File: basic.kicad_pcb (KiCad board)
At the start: 4 copper layers, 60 x 80 mm, 96 parts, among them CON1 MSATA-PCIE_MINI-CARD-MM60-52B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, J2 simcard, J3 Conn_01x02_Male, J4 Conn_01x02_Male, J5 Conn_02x02_Top_Bottom, Q1 DMP3099L-7, Q3 MBT3904DW1, SW1 SW_Push, U1 ESP32-WROOM-32U, U2 MCP2515-QFN, U3 TPS565201DDC, U4 TCAN332, U5 MCP73223-C2S, U6 MIC94085, U7 MMA8452Q, U8 TPS22810DRV, U9 TC2030_SWD, X1 dummy, X2 dummy, Y2 M8AIG-16-12-2T3

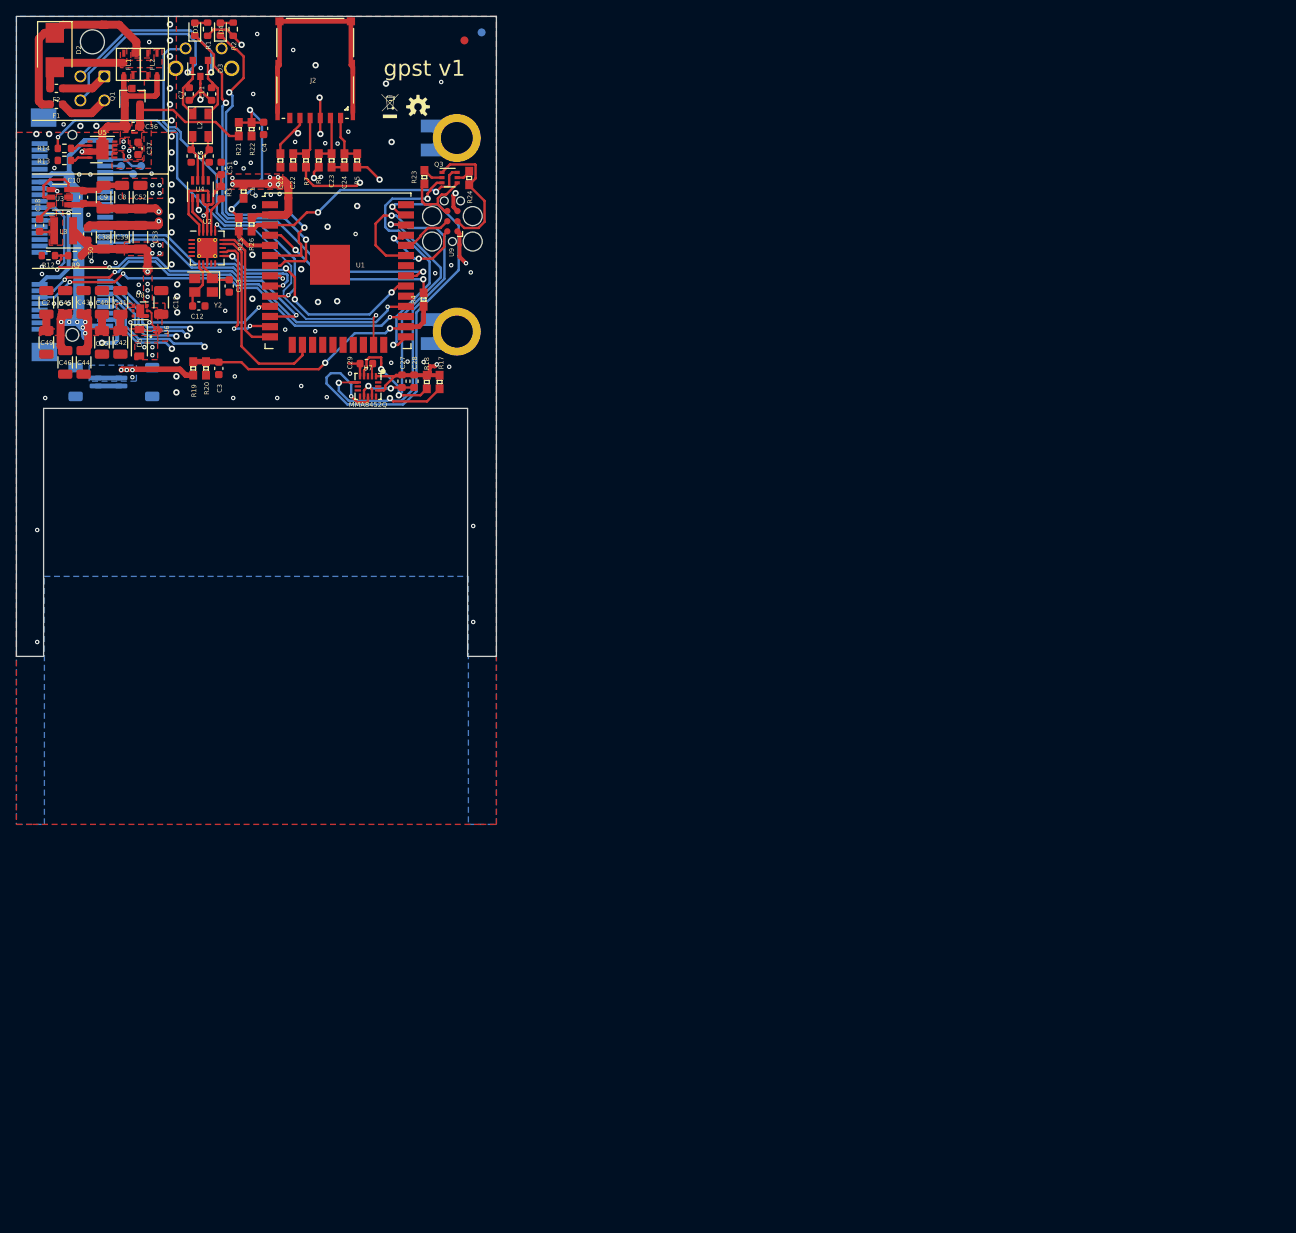
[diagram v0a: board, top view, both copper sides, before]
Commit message: Power section placement completed.
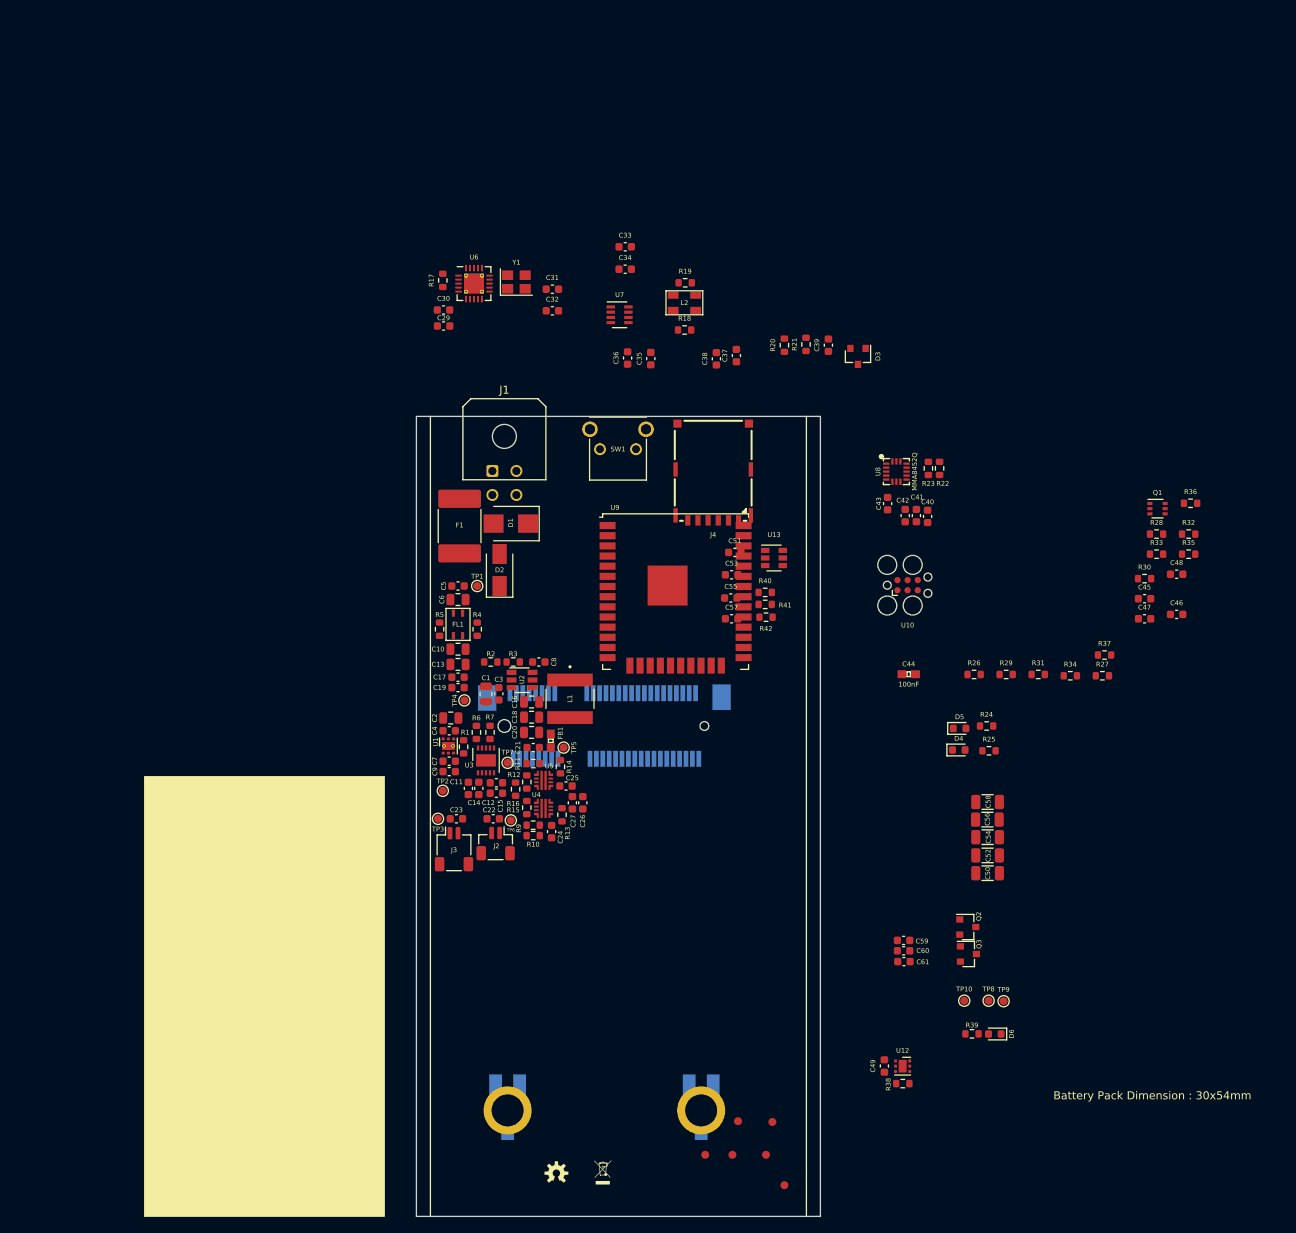
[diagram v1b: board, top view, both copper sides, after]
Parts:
- removed C28: 0.1uF, Capacitor_SMD:C_0603_1608Metric
- removed F2: C2Q 4, Fuse:Fuse_0603_1608Metric
- removed FL2: BACKUP ACP3225-501-2P-T000, aep:ACP3225
- removed J5: Conn_02x02_Top_Bottom, Connector_Molex:Molex_Micro-Fit_3.0_43045-0400_2x02_P3.00mm_Horizontal
- removed L3: 2.2uH, Inductor_SMD:L_Coilcraft_XxL4020
- removed Y2: M8AIG-16-12-2T3, Crystal:Crystal_SMD_Abracon_ABM8G-4Pin_3.2x2.5mm
- added C14: 100nF, Capacitor_SMD:C_0603_1608Metric, F.Cu at (57.8, 96.5)
- added C16: 22uF 25V, Capacitor_SMD:C_0805_2012Metric, F.Cu at (64.4, 85.7)
- added C17: 100nF 50V, Capacitor_SMD:C_0603_1608Metric, F.Cu at (55.2, 82.6)
- added C19: 100pF 50V, Capacitor_SMD:C_0603_1608Metric, F.Cu at (55.2, 83.9)
- added C20: 22uF 25V, Capacitor_SMD:C_0805_2012Metric, F.Cu at (64.4, 89.5)
- added C21: 100pF 50V, Capacitor_SMD:C_0603_1608Metric, F.Cu at (64.6, 91.4)
- added C26: 100nF, Capacitor_SMD:C_0603_1608Metric, F.Cu at (70.8, 98.3)
- added C30: 10uF, Capacitor_SMD:C_0603_1608Metric, F.Cu at (53.4, 36.7)
- added C31: 33pf, Capacitor_SMD:C_0603_1608Metric, F.Cu at (67.0, 34.1)
- added C32: 33pf, Capacitor_SMD:C_0603_1608Metric, F.Cu at (67.0, 36.8)
- added C33: 100nF, Capacitor_SMD:C_0603_1608Metric, F.Cu at (76.1, 28.8)
- added C34: 10uF, Capacitor_SMD:C_0603_1608Metric, F.Cu at (76.1, 31.6)
- added C47: 100nF, Capacitor_SMD:C_0603_1608Metric, F.Cu at (141.0, 75.3)
- added C48: 100nF, Capacitor_SMD:C_0603_1608Metric, F.Cu at (145.0, 69.7)
- added C54: 100uF, Capacitor_SMD:C_1206_3216Metric, F.Cu at (121.4, 102.6)
- added C55: 33pF, Capacitor_SMD:C_0603_1608Metric, F.Cu at (89.3, 72.7)
- added C56: 100uF, Capacitor_SMD:C_1206_3216Metric, F.Cu at (121.4, 100.4)
- added C57: 100nF, Capacitor_SMD:C_0603_1608Metric, F.Cu at (89.4, 75.3)
- added C58: 100uF, Capacitor_SMD:C_1206_3216Metric, F.Cu at (121.4, 98.2)
- added C59: 100nF, Capacitor_SMD:C_0603_1608Metric, F.Cu at (110.9, 115.5)
- added C60: 33pF, Capacitor_SMD:C_0603_1608Metric, F.Cu at (110.9, 116.8)
- added C61: 10pF, Capacitor_SMD:C_0603_1608Metric, F.Cu at (110.9, 118.2)
- added D6: APGA1602CGC/KA, LED_SMD:LED_0603_1608Metric, F.Cu at (122.3, 127.2)
- added FB1: BLM18PG181SN1D, Capacitors:0603, F.Cu at (66.8, 90.6)
- added FID3: Fiducial, Aesthetics:FIDUCIAL-1X2, F.Cu at (94.5, 138.2)
- added FID4: Fiducial, Aesthetics:FIDUCIAL-1X2, F.Cu at (86.1, 142.3)
- added FID5: Fiducial, Aesthetics:FIDUCIAL-1X2, F.Cu at (89.5, 142.3)
- added FID6: Fiducial, Aesthetics:FIDUCIAL-1X2, F.Cu at (93.7, 142.3)
- added J1: Conn_02x02_Top_Bottom, Connector_Molex:Molex_Micro-Fit_3.0_43045-0400_2x02_P3.00mm_Horizontal, F.Cu at (59.5, 56.8)
- added L1: 1255AY-3R9N=P3, 1255AY-3R9N_P3:IND_1255AY-3R9N=P3, F.Cu at (69.2, 85.3)
- added Q2: MMUN2233LT1G, Package_TO_SOT_SMD:SOT-23, F.Cu at (118.9, 113.8)
- added R10: 68K, Resistor_SMD:R_0603_1608Metric, F.Cu at (64.6, 102.4)
- added R11: 51K, Resistor_SMD:R_0603_1608Metric, F.Cu at (64.6, 93.4)
- added R15: 10k, Resistor_SMD:R_0603_1608Metric, F.Cu at (63.8, 98.9)
- added R16: 10k, Resistor_SMD:R_0603_1608Metric, F.Cu at (62.4, 96.6)
- added R27: R0, Resistor_SMD:R_0603_1608Metric, F.Cu at (135.8, 82.4)
- added R28: 10K, Resistor_SMD:R_0603_1608Metric, F.Cu at (142.5, 64.7)
- added R29: R0, Resistor_SMD:R_0603_1608Metric, F.Cu at (123.7, 82.3)
- added R30: 10K, Resistor_SMD:R_0603_1608Metric, F.Cu at (141.0, 70.3)
- added R31: 10K, Resistor_SMD:R_0603_1608Metric, F.Cu at (127.7, 82.3)
- added R32: 1K, Resistor_SMD:R_0603_1608Metric, F.Cu at (146.5, 64.7)
- added R33: 1K, Resistor_SMD:R_0603_1608Metric, F.Cu at (142.5, 67.2)
- added R34: 22K, Resistor_SMD:R_0603_1608Metric, F.Cu at (131.7, 82.4)
- added R35: 5K, Resistor_SMD:R_0603_1608Metric, F.Cu at (146.5, 67.2)
- added R36: 22K, Resistor_SMD:R_0603_1608Metric, F.Cu at (146.8, 60.9)
- added R37: 5K, Resistor_SMD:R_0603_1608Metric, F.Cu at (136.0, 79.8)
- added R38: R0-DNP, Resistor_SMD:R_0603_1608Metric, F.Cu at (110.8, 133.4)
- added R39: 1K, Resistor_SMD:R_0603_1608Metric, F.Cu at (119.5, 127.2)
- added R40: 22R, Resistor_SMD:R_0603_1608Metric, F.Cu at (93.6, 72.0)
- added R41: 22R, Resistor_SMD:R_0603_1608Metric, F.Cu at (93.6, 73.5)
- added R42: 22R, Resistor_SMD:R_0603_1608Metric, F.Cu at (93.7, 75.1)
- added TP1: L0, TestPoint:TestPoint_Pad_D1.0mm, F.Cu at (57.6, 71.2)
- added TP10: L0, TestPoint:TestPoint_Pad_D1.0mm, F.Cu at (118.5, 123.0)
- added TP5: L0, TestPoint:TestPoint_Pad_D1.0mm, F.Cu at (68.4, 91.4)
- added TP6: L0, TestPoint:TestPoint_Pad_D1.0mm, F.Cu at (61.8, 100.5)
- added TP7: L0, TestPoint:TestPoint_Pad_D1.0mm, F.Cu at (61.4, 93.3)
- added TP8: L0, TestPoint:TestPoint_Pad_D1.0mm, F.Cu at (121.5, 123.0)
- added TP9: L0, TestPoint:TestPoint_Pad_D1.0mm, F.Cu at (123.4, 123.1)
- added U10: TC2030_SWD, Connector:Tag-Connect_TC2030-IDC-FP_2x03_P1.27mm_Vertical, F.Cu at (111.4, 71.1)
- added U12: TPS22810DRV, Package_SON:WSON-6-1EP_2x2mm_P0.65mm_EP1x1.6mm, F.Cu at (110.8, 131.2)
- added U13: USBLC6-4SC6, Package_TO_SOT_SMD:SOT-23-6, F.Cu at (94.7, 67.7)
- added Y1: M8AIG-16-12-2T3, Crystal:Crystal_SMD_Abracon_ABM8G-4Pin_3.2x2.5mm, F.Cu at (62.5, 33.2)
- C1: value 2.2uF -> 10uF 50V; footprint Capacitors:0603 -> Capacitor_SMD:C_0805_2012Metric
- C10: value 100nF 50V -> 10uF 50V; footprint Capacitor_SMD:C_0603_1608Metric -> Capacitor_SMD:C_0805_2012Metric
- C11: value 56pf -> 4.7uF
- C12: value 33pf -> 4.7uF
- C13: value 33pf -> 10uF 50V; footprint Capacitor_SMD:C_0603_1608Metric -> Capacitor_SMD:C_0805_2012Metric
- C15, C41, C42, C43, C45: value 10uF -> 100nF; footprint Capacitor_SMD:C_1206_3216Metric -> Capacitor_SMD:C_0603_1608Metric
- C18: value 100nF 50V -> 22uF 25V; footprint Capacitor_SMD:C_0603_1608Metric -> Capacitor_SMD:C_0805_2012Metric
- C2: value 10uF -> 10uF 50V; footprint Capacitor_SMD:C_1206_3216Metric -> Capacitor_SMD:C_0805_2012Metric
- C22, C23: value 33pF -> 4.7uF; footprint Capacitors:0603 -> Capacitor_SMD:C_0603_1608Metric
- C24: value 33pF -> 1nF; footprint Capacitors:0603 -> Capacitor_SMD:C_0603_1608Metric
- C25: value 100nF -> 1nF; footprint Capacitors:0603 -> Capacitor_SMD:C_0603_1608Metric
- C27: value 4.7uF -> 10uF
- C29: value 0.1uF -> 100nF
- C3, C4: value 100nF -> 100nF 50V
- C35: value 10uF -> 56pf; footprint Capacitor_SMD:C_1206_3216Metric -> Capacitor_SMD:C_0603_1608Metric
- C36, C37: value 4.7uF 50V -> 56pf
- C38: value 100uF -> 56pf; footprint Capacitor_SMD:C_1206_3216Metric -> Capacitor_SMD:C_0603_1608Metric
- C39: value 100uF -> 56pf-DNP; footprint Capacitor_SMD:C_1206_3216Metric -> Capacitor_SMD:C_0603_1608Metric
- C40: value 10uF -> 4.7uF; footprint Capacitor_SMD:C_1206_3216Metric -> Capacitor_SMD:C_0603_1608Metric
- C44: value 10uF -> 100nF; footprint Capacitor_SMD:C_1206_3216Metric -> Capacitors:0603
- C46, C49: footprint Capacitor_SMD:C_1206_3216Metric -> Capacitor_SMD:C_0603_1608Metric
- C5: value 56pf -> 100pF 50V
- C50: value 2.2uF 50V -> 100uF; footprint Capacitor_SMD:C_0603_1608Metric -> Capacitor_SMD:C_1206_3216Metric
- C51: value 100nF 50V -> 33pF
- C53: value 100uF -> 33pF; footprint Capacitor_SMD:C_1206_3216Metric -> Capacitor_SMD:C_0603_1608Metric
- C6: value 56pf -> 10uF 50V; footprint Capacitor_SMD:C_0603_1608Metric -> Capacitor_SMD:C_0805_2012Metric
- C7: value 56pf -> 100nF
- C8: value 100uF -> 100nF 50V; footprint Capacitor_SMD:C_1206_3216Metric -> Capacitor_SMD:C_0603_1608Metric
- C9: value 100uF -> 4.7uF; footprint Capacitor_SMD:C_1206_3216Metric -> Capacitor_SMD:C_0603_1608Metric
- D1: value APGA1602QBC/KA-5MAV -> SMBJ16CA-Q; footprint LED_SMD:LED_0603_1608Metric -> Diode_SMD:D_SMB
- D2: value SMBJ16CA-13-F -> RS1GTR; footprint Diode_SMD:D_SMB -> Diode_SMD:D_SMA
- D4: value APGA1602CGC/KA -> APGA1602QBC/KA-5MAV
- D5: value DNP Backup -> APGA1602CGC/KA; footprint Diode_SMD:D_SOD-123 -> LED_SMD:LED_0603_1608Metric
- F1: value C2Q 4 -> 0ZCF0050FF2C; footprint Fuse:Fuse_0603_1608Metric -> Fuse:Fuse_2920_7451Metric_Castellated
- FID2, J3, SW1: moved to F.Cu
- J2: value simcard -> Conn_01x02_Male; footprint aep:nanosim-Wurth-693043020611 -> Connector_JST:JST_SH_BM02B-SRSS-TB_1x02-1MP_P1.00mm_Vertical
- J4: value Conn_01x02_Male -> simcard; footprint Connector_JST:JST_SH_BM02B-SRSS-TB_1x02-1MP_P1.00mm_Vertical -> aep:nanosim-Wurth-693043020611; moved to F.Cu
- Q1: value DMP3099L-7 -> MBT3904DW1; footprint Package_TO_SOT_SMD:SOT-23 -> Package_TO_SOT_SMD:SOT-363_SC-70-6
- Q3: value MBT3904DW1 -> MMUN2233LT1G; footprint Package_TO_SOT_SMD:SOT-363_SC-70-6 -> Package_TO_SOT_SMD:SOT-23
- R1: value 1K -> 10k
- R12: value 10K -> 33K
- R17: value 3k6 -> 10k; footprint Resistors:0603 -> Resistor_SMD:R_0603_1608Metric
- R18: value 3k6 -> R0-DNP; footprint Resistors:0603 -> Resistor_SMD:R_0603_1608Metric
- R19: value 22K -> R0-DNP; footprint Resistors:0603 -> Resistor_SMD:R_0603_1608Metric
- R2: value 1K -> R0-DNP
- R20: value 5K -> 10k-DNP; footprint Resistors:0603 -> Resistor_SMD:R_0603_1608Metric
- R21: value 22K -> 10k-DNP; footprint Resistors:0603 -> Resistor_SMD:R_0603_1608Metric
- R22: value 5K -> 10k; footprint Resistors:0603 -> Resistor_SMD:R_0603_1608Metric
- R23: value 10K -> 10k; footprint Resistors:0603 -> Resistor_SMD:R_0603_1608Metric
- R24: value 10K -> 1K; footprint Resistors:0603 -> Resistor_SMD:R_0603_1608Metric
- R25: value R0 -> 1K; footprint Resistors:0603 -> Resistor_SMD:R_0603_1608Metric
- R26: value 10K -> R0; footprint Resistors:0603 -> Resistor_SMD:R_0603_1608Metric
- R3: value 1K-10K -> R0
- R4: value R0 -> R0-DNP; footprint Resistors:0603 -> Resistor_SMD:R_0603_1608Metric
- R5: value 45 -> R0-DNP; footprint Resistors:0603 -> Resistor_SMD:R_0603_1608Metric
- R6: value 45 -> 3.9k; footprint Resistors:0603 -> Resistor_SMD:R_0603_1608Metric
- R7: value 45 -> 10k; footprint Resistors:0603 -> Resistor_SMD:R_0603_1608Metric
- R9: value 33K2 -> 100K
- TP2: footprint OLIMEX_TestPoints-FP:TP_SMD -> TestPoint:TestPoint_Pad_D1.0mm; moved to F.Cu
- TP3: value L1 -> L0; footprint OLIMEX_TestPoints-FP:TP_SMD -> TestPoint:TestPoint_Pad_D1.0mm; moved to F.Cu
- TP4: value L3 -> L0; footprint OLIMEX_TestPoints-FP:TP_SMD -> TestPoint:TestPoint_Pad_D1.0mm; moved to F.Cu
- U1: value ESP32-WROOM-32U -> TLV76750; footprint RF_Module:ESP32-WROOM-32U -> Package_SON:WSON-6-1EP_2x2mm_P0.65mm_EP1x1.6mm_ThermalVias
- U2: value MCP2515-QFN -> AP63203WU; footprint Package_DFN_QFN:QFN-20-1EP_4x4mm_P0.5mm_EP2.5x2.5mm_ThermalVias -> Package_TO_SOT_SMD:TSOT-23-6
- U3: value TPS565201DDC -> MCP73123-22S; footprint Package_TO_SOT_SMD:SOT-23-6 -> Package_DFN_QFN:DFN-10-1EP_3x3mm_P0.5mm_EP1.55x2.48mm
- U4: value TCAN332 -> LM73100; footprint Package_TO_SOT_SMD:SOT-23-8 -> artanis-light:LM73100
- U5: value MCP73223-C2S -> LM73100; footprint Package_DFN_QFN:DFN-10-1EP_3x3mm_P0.5mm_EP1.55x2.48mm -> artanis-light:LM73100
- U6: value MIC94085 -> MCP2515-QFN; footprint aep:IC_MIC94080YFT-TR -> Package_DFN_QFN:QFN-20-1EP_4x4mm_P0.5mm_EP2.5x2.5mm_ThermalVias
- U7: value MMA8452Q -> TCAN332; footprint Silicon-Custom:QFN-16 -> Package_TO_SOT_SMD:SOT-23-8
- U8: value TPS22810DRV -> MMA8452Q; footprint Package_SON:WSON-6-1EP_2x2mm_P0.65mm_EP1x1.6mm -> Silicon-Custom:QFN-16
- U9: value TC2030_SWD -> ESP32-WROOM-32U; footprint Connector:Tag-Connect_TC2030-IDC-FP_2x03_P1.27mm_Vertical -> RF_Module:ESP32-WROOM-32U
- moved FID1 148.6 mm to (96.0, 146.1)
- moved C46 142.5 mm to (145.0, 74.8), turned to 0 degrees
- moved C45 139.9 mm to (141.0, 72.8), turned to 0 degrees
- moved FID2 139.8 mm to (90.2, 138.1)
- moved C49 138.4 mm to (108.5, 131.2)
- moved Q1 138.1 mm to (142.6, 61.5), turned to 0 degrees
- moved C50 138.0 mm to (121.4, 107.1), turned to 0 degrees
- moved X1 135.9 mm to (73.3, 144.5)
- moved X2 134.4 mm to (67.5, 144.6)
- moved C52 134.1 mm to (121.4, 104.9), turned to 0 degrees
- moved D4 129.0 mm to (117.8, 91.7), turned to 0 degrees
- moved Q3 116.7 mm to (119.0, 117.2)
- moved R25 114.6 mm to (121.6, 91.8), turned to 0 degrees
- moved D5 113.3 mm to (117.9, 89.0), turned to 0 degrees
- moved C44 110.3 mm to (111.5, 82.2), turned to 0 degrees
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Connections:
- C1 pad 1: 3.3V -> GND
- C1 pad 2: GND -> +12V
- C10 pad 2: VBAT -> +12V
- C11 pad 1: CAN0- -> +5V
- C12 pad 1: /xtalc0- -> +BATT
- C13 pad 2: /xtalc0+ -> +12V
- C15 pad 1: GND -> +BATT
- C15 pad 2: 3.3V -> GND
- C18 pad 1: Net-(C18-Pad1) -> GND
- C18 pad 2: /power/SW -> Net-(C16-Pad2)
- C2 pad 2: MODEM_3.3V -> +12V
- C22 pad 1: /sim_reset -> +BATT
- C23 pad 1: /sim_clk -> +BATT
- C24 pad 1: /sim_data -> Net-(C24-Pad1)
- C25 pad 1: /sim_vcc -> Net-(C25-Pad1)
- C27 pad 1: 3.3V -> +3V3
- C29 pad 1: Net-(C29-Pad1) -> +3V3
- C3 pad 2: SENSE_VBAT -> +12V
- C35 pad 2: MODEM_3.3V -> /canbus/CANL0
- C36 pad 2: V12_safe -> /canbus/CANH0
- C37 pad 2: VBAT -> CANL
- C38 pad 2: 3.3V -> CANH
- C39 pad 2: 3.3V -> Net-(C39-Pad2)
- C4 pad 2: SENSE_V12 -> +12V
- C40 pad 1: GND -> +3V3
- C40 pad 2: MODEM_3.3V -> GND
- C41 pad 1: GND -> +3V3
- C41 pad 2: MODEM_3.3V -> GND
- C42 pad 2: MODEM_3.3V -> +3V3
- C43 pad 1: GND -> Net-(C43-Pad1)
- C43 pad 2: MODEM_3.3V -> GND
- C44 pad 2: MODEM_3.3V -> +3V3
- C45 pad 1: GND -> +3V3
- C45 pad 2: MODEM_3.3V -> GND
- C46 pad 1: GND -> +3V3
- C46 pad 2: MODEM_3.3V -> GND
- C49 pad 1: GND -> +3V3
- C49 pad 2: MODEM_3.3V -> GND
- C5 pad 1: /c2+ -> VIN_GND
- C5 pad 2: GND -> /power/12V_FILTER_IN
- C50 pad 1: GND -> MODEM_3.3V
- C50 pad 2: 3.3V -> GND
- C51 pad 1: GND -> /modem/sim_reset
- C51 pad 2: 3.3V -> GND
- C52 pad 1: GND -> MODEM_3.3V
- C52 pad 2: VBAT -> GND
- C53 pad 1: GND -> /modem/sim_clk
- C53 pad 2: 3.3V -> GND
- C6 pad 1: /c2- -> VIN_GND
- C6 pad 2: GND -> /power/12V_FILTER_IN
- C7 pad 1: CAN0+ -> +5V
- C8 pad 1: GND -> Net-(C8-Pad1)
- C8 pad 2: VBAT -> Net-(C8-Pad2)
- C9 pad 1: GND -> +5V
- C9 pad 2: VBAT -> GND
- CON1 pad 1: (no net) -> Net-(CON1-Pad1)
- CON1 pad 11: MODEM_TX -> /esp32/MODEM_RX
- CON1 pad 13: MODEM_RX -> /esp32/MODEM_TX
- CON1 pad 16: /sim_vpp -> Net-(CON1-Pad16)
- CON1 pad 17: (no net) -> /modem/MODEM_RI
- CON1 pad 19: (no net) -> Net-(CON1-Pad19)
- CON1 pad 20: MODEM_WDISABLE -> /modem/W_DISABLE
- CON1 pad 22: MODEM_RESET -> /modem/PERST
- CON1 pad 23: (no net) -> Net-(CON1-Pad23)
- CON1 pad 25: (no net) -> Net-(CON1-Pad25)
- CON1 pad 28: (no net) -> Net-(CON1-Pad28)
- CON1 pad 3: (no net) -> Net-(CON1-Pad3)
- CON1 pad 30: (no net) -> Net-(CON1-Pad30)
- CON1 pad 31: MODEM_DTR -> /esp32/MODEM_DTR
- CON1 pad 32: (no net) -> Net-(CON1-Pad32)
- CON1 pad 33: (no net) -> Net-(CON1-Pad33)
- CON1 pad 36: (no net) -> /modem/USB_DM
- CON1 pad 37: (no net) -> GND
- CON1 pad 38: (no net) -> /modem/USB_DP
- CON1 pad 42: Net-(CON1-Pad42) -> /modem/LED_WWAN
- CON1 pad 43: (no net) -> GND
- CON1 pad 45: (no net) -> Net-(CON1-Pad45)
- CON1 pad 47: (no net) -> Net-(CON1-Pad47)
- CON1 pad 48: (no net) -> Net-(CON1-Pad48)
- CON1 pad 49: (no net) -> Net-(CON1-Pad49)
- CON1 pad 5: (no net) -> Net-(CON1-Pad5)
- CON1 pad 51: (no net) -> Net-(CON1-Pad51)
- CON1 pad 6: (no net) -> Net-(CON1-Pad6)
- CON1 pad 7: (no net) -> Net-(CON1-Pad7)
- CON1 pad 8: /sim_vcc -> /modem/sim_vcc
- D1 pad 1: LED_BLUE -> Net-(D1-Pad1)
- D1 pad 2: Net-(D1-Pad2) -> VIN_GND
- D2 pad 1: /power/12v_prefilter+ -> /power/12V_FILTER_IN
- D2 pad 2: /power/12v_prefilter- -> Net-(D1-Pad1)
- D3 pad 1: CAN0- -> CANL
- D3 pad 2: CAN0+ -> CANH
- D4 pad 1: LED_GREEN -> /esp32/LED_GREEN
- D5 pad 1: MODEM_3.3V -> /esp32/LED_BLUE
- D5 pad 2: 3.3V -> Net-(D5-Pad2)
- F1 pad 1: BATT+ -> Net-(D1-Pad1)
- F1 pad 2: /power/12v_prefilter+ -> VIN_12V
- FL1 pad 1: /power/12v_postfilter+ -> +12V
- FL1 pad 3: /power/12v_prefilter- -> VIN_GND
- FL1 pad 4: /power/12v_prefilter+ -> /power/12V_FILTER_IN
- J3 pad 1: VBAT -> +BATT
- L2 pad 1: /c2- -> /canbus/CANL0
- L2 pad 2: /c2+ -> /canbus/CANH0
- L2 pad 3: CAN0+ -> CANH
- L2 pad 4: CAN0- -> CANL
- Q1 pad 1: GND -> FTDI_CTS
- Q1 pad 2: V12_safe -> Net-(Q1-Pad2)
- Q1 pad 3: /power/12v_postfilter+ -> CPU_BOOT
- Q3 pad 1: FTDI_CTS -> /esp32/MODEM_RESET
- Q3 pad 2: Net-(Q3-Pad2) -> GND
- Q3 pad 3: CPU_BOOT -> /modem/PERST
- R1 pad 1: 3.3V -> /esp32/CHARGER_EN
- R1 pad 2: Net-(D1-Pad2) -> GND
- R12 pad 1: Net-(R12-Pad1) -> GND
- R12 pad 2: GND -> /power/3V3_PG
- R14 pad 2: CHARGE_STAT -> GND
- R17 pad 1: TWI0_SDA -> Net-(R17-Pad1)
- R17 pad 2: 3.3V -> +3V3
- R18 pad 1: TWI0_SCK -> /canbus/CANH0
- R18 pad 2: 3.3V -> CANH
- R19 pad 1: VBAT -> CANL
- R19 pad 2: SENSE_VBAT -> /canbus/CANL0
- R2 pad 1: 3.3V -> Net-(R2-Pad1)
- R2 pad 2: Net-(D4-Pad2) -> GND
- R20 pad 1: SENSE_VBAT -> CANL
- R20 pad 2: GND -> Net-(C39-Pad2)
- R21 pad 1: V12_safe -> CANH
- R21 pad 2: SENSE_V12 -> Net-(C39-Pad2)
- R22 pad 1: SENSE_V12 -> /esp32/TWIO_SCK
- R22 pad 2: GND -> +3V3
- R23 pad 1: FTDI_DTR -> /esp32/TWIO_SDA
- R23 pad 2: Net-(Q3-Pad2) -> +3V3
- R24 pad 1: FTDI_CTS -> +3V3
- R24 pad 2: Net-(Q3-Pad5) -> Net-(D4-Pad2)
- R25 pad 1: SENSE_V12 -> +3V3
- R25 pad 2: Net-(R25-Pad2) -> Net-(D5-Pad2)
- R26 pad 1: CPU_ENABLE -> /esp32/SENSE_VBAT
- R26 pad 2: 3.3V -> Net-(R26-Pad2)
- R3 pad 1: Net-(R3-Pad1) -> Net-(R2-Pad1)
- R3 pad 2: 3.3V -> /power/3V3_BUCK
- R4 pad 1: SENSE_VBAT -> /power/12V_FILTER_IN
- R4 pad 2: Net-(R4-Pad2) -> +12V
- R5 pad 1: /sim_data -> GND
- R5 pad 2: Net-(CON1-Pad10) -> VIN_GND
- R6 pad 1: /sim_clk -> GND
- R6 pad 2: Net-(CON1-Pad12) -> Net-(R6-Pad2)
- R7 pad 1: /sim_reset -> /esp32/CHARGE_STAT
- R7 pad 2: Net-(CON1-Pad14) -> +3V3
- R9 pad 1: 3.3V -> Net-(R10-Pad2)
- R9 pad 2: Net-(R12-Pad1) -> +BATT
- TP2 pad 1: Net-(CON1-Pad42) -> +5V
- TP3 pad 1: Net-(CON1-Pad44) -> +BATT
- TP4 pad 1: Net-(CON1-Pad46) -> +12V
- U1 pad 1: GND -> +5V
- U1 pad 2: 3.3V -> +5V
- U1 pad 3: CPU_ENABLE -> GND
- U1 pad 4: Net-(R4-Pad2) -> /esp32/CHARGER_EN
- U1 pad 5: Net-(R25-Pad2) -> GND
- U1 pad 6: LED_GREEN -> +12V
- U1 pad 7: LED_BLUE -> GND
- U2 pad 1: (no net) -> Net-(R2-Pad1)
- U2 pad 2: (no net) -> +12V
- U2 pad 3: (no net) -> +12V
- U2 pad 4: (no net) -> GND
- U2 pad 5: (no net) -> Net-(C8-Pad1)
- U2 pad 6: /xtalc0- -> Net-(C8-Pad2)
- U3 pad 1: GND -> +5V
- U3 pad 2: /power/SW -> +5V
- U3 pad 3: VBAT -> +BATT
- U3 pad 4: Net-(R12-Pad1) -> +BATT
- U3 pad 5: VBAT -> Net-(U3-Pad5)
- U3 pad 6: Net-(C18-Pad1) -> Net-(U3-Pad6)
- U4 pad 1: Net-(U2-Pad19) -> Net-(R10-Pad2)
- U4 pad 2: GND -> /power/3V3_PG
- U4 pad 3: 3.3V -> /power/IN2_PG
- U4 pad 4: Net-(U2-Pad20) -> Net-(R10-Pad2)
- U4 pad 5: (no net) -> +BATT
- U4 pad 6: /c2- -> +3V3
- U4 pad 7: /c2+ -> Net-(C24-Pad1)
- U4 pad 8: (no net) -> GND
- U5 pad 1: V12_safe -> /power/3V3_PG
- U5 pad 10: Net-(R13-Pad1) -> Net-(U5-Pad10)
- U5 pad 2: V12_safe -> GND
- U5 pad 3: VBAT -> /power/IN1_PG
- U5 pad 4: VBAT -> /power/3V3_PG
- U5 pad 5: (no net) -> /power/3V3_BUCK
- U5 pad 6: (no net) -> +3V3
- U5 pad 7: Net-(R14-Pad1) -> Net-(C25-Pad1)
- U5 pad 9: GND -> Net-(R14-Pad1)
- U6 pad 1: MODEM_3.3V -> Net-(U6-Pad1)
- U6 pad 2: GND -> (no net)
- U6 pad 3: 3.3V -> (no net)
- U6 pad 4: MODEM_RELAIS -> (no net)
- U7 pad 1: 3.3V -> /canbus/TxCAN
- U7 pad 2: Net-(C29-Pad1) -> GND
- U7 pad 3: (no net) -> +3V3
- U7 pad 4: TWI0_SCK -> /canbus/RxCAN
- U7 pad 5: GND -> Net-(U7-Pad5)
- U7 pad 6: TWI0_SDA -> /canbus/CANL0
- U7 pad 7: (no net) -> /canbus/CANH0
- U7 pad 8: (no net) -> Net-(U7-Pad8)
- U8 pad 1: MODEM_3.3V -> +3V3
- U8 pad 2: (no net) -> Net-(C43-Pad1)
- U8 pad 4: GND -> /esp32/TWIO_SCK
- U8 pad 5: MODEM_RELAIS -> GND
- U8 pad 6: 3.3V -> /esp32/TWIO_SDA
- U8 pad 7: GND -> Net-(U8-Pad7)
- U9 pad 1: 3.3V -> GND
- U9 pad 2: FTDI_RXD -> +3V3
- U9 pad 3: FTDI_CTS -> CPU_ENABLE
- U9 pad 4: FTDI_TXD -> Net-(R26-Pad2)
- U9 pad 5: GND -> Net-(R27-Pad2)
- U9 pad 6: FTDI_DTR -> /esp32/LED_GREEN
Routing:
- net GND: track 153.6 -> 0.00 mm, vias 102 -> 0
- net /sim_vcc: track 75.6 -> 0.00 mm, vias 2 -> 0
- net 3.3V: track 74.5 -> 0.00 mm, vias 21 -> 0
- net /sim_vpp: track 71.0 -> 0.00 mm, vias 3 -> 0
- net Net-(CON1-Pad12): track 63.7 -> 0.00 mm, vias 2 -> 0
- net MODEM_3.3V: track 62.1 -> 0.00 mm, vias 6 -> 0
- net Net-(CON1-Pad14): track 61.9 -> 0.00 mm, vias 2 -> 0
- net TWI0_SDA: track 60.5 -> 0.00 mm, vias 3 -> 0
- net Net-(CON1-Pad10): track 58.1 -> 0.00 mm, vias 2 -> 0
- net softreset: track 57.5 -> 0.00 mm, vias 1 -> 0
- net IMU_INT1: track 56.8 -> 0.00 mm, vias 2 -> 0
- net MODEM_RX: track 51.5 -> 0.00 mm, vias 3 -> 0
- net MODEM_TX: track 50.2 -> 0.00 mm, vias 3 -> 0
- net CHARGE_STAT: track 49.5 -> 0.00 mm, vias 2 -> 0
- net MODEM_DTR: track 47.3 -> 0.00 mm, vias 3 -> 0
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- removed copper zone on F.Cu, net /power/12v_postfilter+
- removed copper zone on F.Cu, net /power/12v_prefilter+
- removed copper zone on F.Cu, net /power/12v_prefilter-
- removed copper zone on F.Cu, net /power/SW
- removed copper zone on F.Cu, net 3.3V
- removed copper zone on In2.Cu, net 3.3V
- removed copper zone on B.Cu, net GND
- removed copper zone on F.Cu, net GND
- removed copper zone on In1.Cu, net GND
- removed copper zone on F.Cu, net MODEM_3.3V
- removed copper zone on F.Cu, net V12_safe
- removed copper zone on B.Cu, net VBAT
- removed copper zone on F.Cu, net VBAT
- removed copper zone on In2.Cu, net VBAT
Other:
- board size 60 x 80 mm -> 50.5 x 100 mm
- board text added: "Battery Pack Dimension : 30x54mm"
- board text removed: "gpst v1"

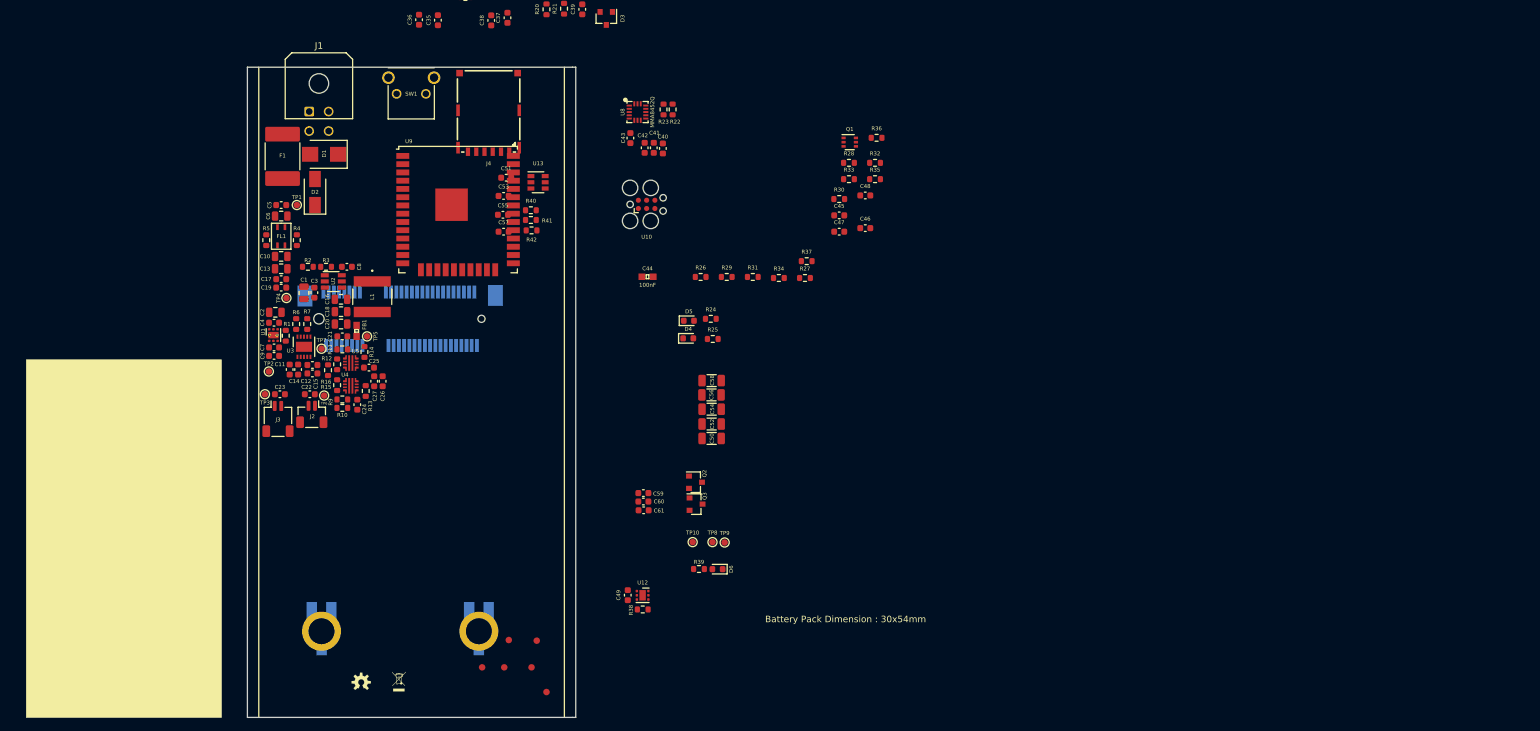
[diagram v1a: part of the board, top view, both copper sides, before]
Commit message: Power section routing completed.
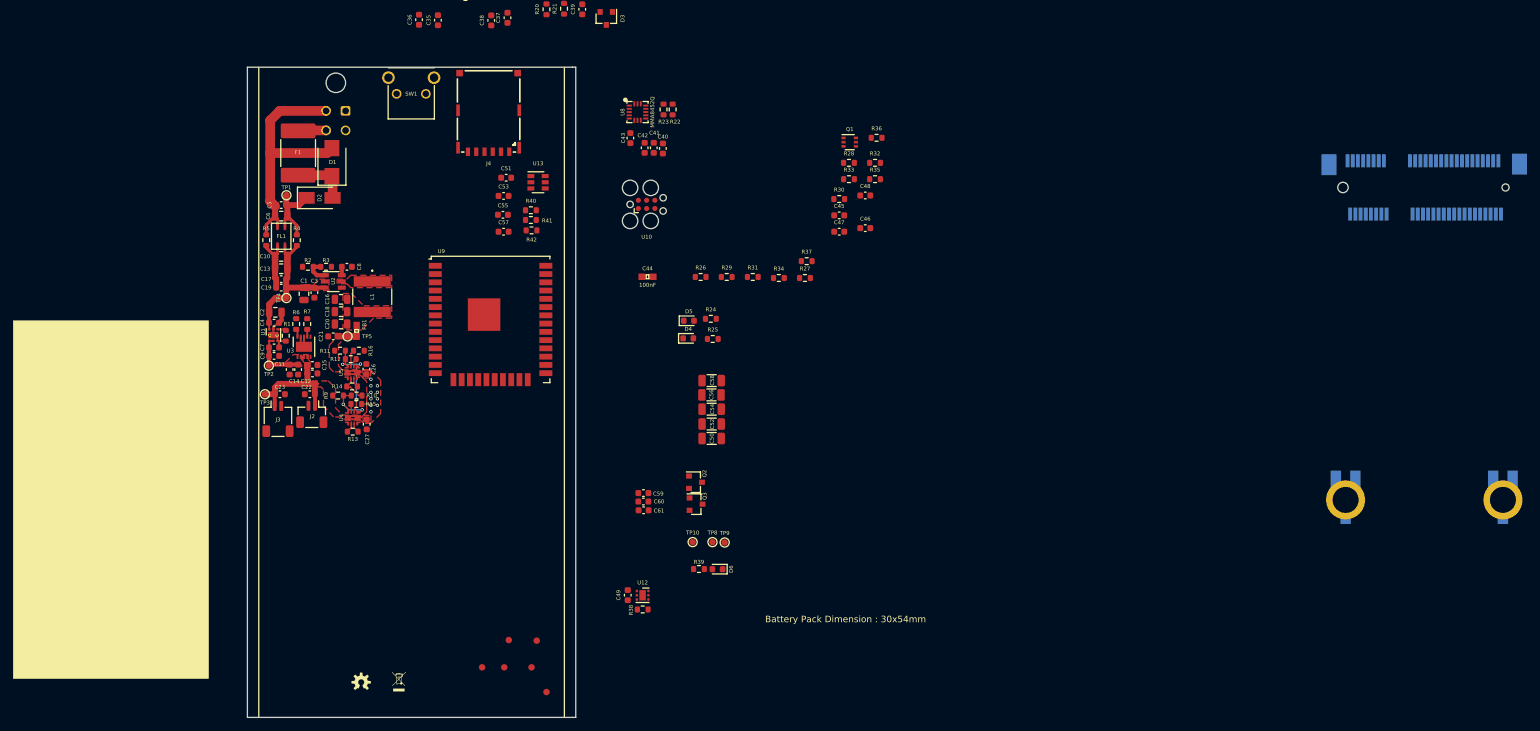
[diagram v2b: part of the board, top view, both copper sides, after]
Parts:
- removed C24, C25: 1nF, Capacitor_SMD:C_0603_1608Metric
- removed TP6, TP7: L0, TestPoint:TestPoint_Pad_D1.0mm
- C26: value 100nF -> 10uF
- J1: moved to B.Cu
- moved CON1 158.8 mm to (231.0, 68.5)
- moved U9 17.6 mm to (87.4, 88.8)
- moved C27 6.72 mm to (68.3, 104.9)
- moved R13 6.56 mm to (66.2, 106.0), turned to 180 degrees
- moved R14 5.63 mm to (66.1, 99.1), turned to 180 degrees
- moved R16 5.62 mm to (67.2, 93.6), turned to 0 degrees
- moved J1 5.60 mm to (65.1, 56.7), turned to 180 degrees
- moved U4 4.91 mm to (66.2, 103.9), turned to 270 degrees
- moved R15 4.14 mm to (66.8, 101.8), turned to 0 degrees
- moved C26 3.12 mm to (68.3, 96.4), turned to 90 degrees
- moved TP5 3.00 mm to (65.4, 91.4)
- moved R10 2.91 mm to (66.8, 100.5)
- moved F1 2.45 mm to (57.8, 63.2)
- moved R12 2.25 mm to (65.9, 94.9), turned to 180 degrees
- moved TP1 2.19 mm to (56.0, 69.7)
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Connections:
- J1 pad 1: VIN_GND -> CANL
- J1 pad 2: CANL -> VIN_GND
- J1 pad 3: VIN_12V -> CANH
- J1 pad 4: CANH -> VIN_12V
- Y1 pad 2: GND -> (no net)
- Y1 pad 4: GND -> (no net)
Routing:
- net VIN_GND: track 0.00 -> 39.6 mm
- net GND: track 0.00 -> 26.9 mm
- net +12V: track 0.00 -> 23.5 mm
- net +BATT: track 0.00 -> 17.9 mm
- net /power/3V3_PG: track 0.00 -> 14.1 mm, vias 0 -> 3
- net /power/12V_FILTER_IN: track 0.00 -> 12.2 mm
- net +5V: track 0.00 -> 9.06 mm
- net Net-(D1-Pad1): track 0.00 -> 8.65 mm
- net Net-(R10-Pad2): track 0.00 -> 8.13 mm, vias 0 -> 2
- net VIN_12V: track 0.00 -> 4.33 mm
- net /power/3V3_BUCK: track 0.00 -> 4.25 mm
- net Net-(R2-Pad1): track 0.00 -> 3.89 mm
- net /power/IN1_PG: track 0.00 -> 2.62 mm
- net +3V3: track 0.00 -> 1.62 mm, vias 0 -> 7
- net Net-(R13-Pad1): track 0.00 -> 1.50 mm
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- added copper zone on F.Cu, net (none)
- added copper zone on F.Cu, net +12V
- added copper zone on F.Cu, net +3V3
- added copper zone on F.Cu, net +5V
- added copper zone on F.Cu, net +BATT
- added copper zone on F.Cu, net /power/3V3_BUCK
- added copper zone on F.Cu, net Net-(C16-Pad2)
- added copper zone on F.Cu, net Net-(C8-Pad1)
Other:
- net class Default: clearance 0.14224 -> 0.15; trace_width 0.1524 -> 0.2; via_dia 0.8 -> 0.5; via_drill 0.4 -> 0.3
- rule trace_clearance: 0.14224 -> 0.15

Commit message: PCB design updated.
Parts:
- removed TP10: L0, TestPoint:TestPoint_Pad_D1.0mm
- C39: value 56pf-DNP -> 4.7nf-DNP
- C44: footprint Capacitors:0603 -> Capacitor_SMD:C_0603_1608Metric
- C50, C52, C54, C56, C58, C59, C60, C61, FID4, FID5, FID6, SW1, TP8, TP9: moved to B.Cu
- R20, R21: value 10k-DNP -> 60R-DNP
- moved CON1 166.2 mm to (74.2, 123.8), turned to 0 degrees
- moved FID1 103.5 mm to (53.0, 52.0)
- moved FID4 96.2 mm to (53.0, 52.0)
- moved R35 93.0 mm to (63.0, 108.2), turned to 90 degrees
- moved R32 92.9 mm to (64.4, 108.2), turned to 270 degrees
- moved C47 82.1 mm to (65.8, 108.2), turned to 90 degrees
- moved R36 75.2 mm to (73.2, 76.5)
- moved R34 74.7 mm to (61.6, 108.2), turned to 270 degrees
- moved C48 72.5 mm to (73.2, 79.3)
- moved C46 69.4 mm to (76.0, 82.2), turned to 90 degrees
- moved C58 69.0 mm to (56.1, 120.5), turned to 180 degrees
- moved R28 68.9 mm to (76.5, 84.3), turned to 180 degrees
- moved R33 68.2 mm to (75.3, 78.6), turned to 90 degrees
- moved C56 67.7 mm to (56.1, 118.2), turned to 180 degrees
- moved C54 66.7 mm to (56.1, 116.0), turned to 180 degrees
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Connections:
- U8 pad 10: Net-(U8-Pad10) -> GND
- U8 pad 12: Net-(U8-Pad10) -> GND
- Y1 pad 2: (no net) -> GND
- Y1 pad 4: (no net) -> GND
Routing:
- net GND: track 26.9 -> 171.8 mm, vias 0 -> 137
- net /esp32/SENSE_VBAT: track 0.00 -> 57.5 mm, vias 0 -> 5
- net /canbus/CSO: track 0.00 -> 48.0 mm
- net softreset: track 0.00 -> 47.5 mm
- net /esp32/MODEM_RX: track 0.00 -> 45.2 mm, vias 0 -> 1
- net /esp32/CHARGER_EN: track 1.32 -> 45.5 mm, vias 0 -> 2
- net /esp32/MODEM_DTR: track 0.00 -> 40.9 mm, vias 0 -> 1
- net /esp32/MODEM_TX: track 0.00 -> 39.1 mm, vias 0 -> 1
- net /canbus/CAN0IRQ: track 0.00 -> 38.4 mm, vias 0 -> 2
- net /canbus/MISO: track 0.00 -> 37.9 mm, vias 0 -> 2
- net CPU_ENABLE: track 0.00 -> 37.7 mm, vias 0 -> 2
- net /canbus/MOSI: track 0.00 -> 37.0 mm, vias 0 -> 2
- net +3V3: track 1.62 -> 36.0 mm, vias 7 -> 22
- net FTDI_RXD: track 0.00 -> 33.3 mm, vias 0 -> 2
- net /canbus/SCLK: track 0.00 -> 32.9 mm, vias 0 -> 2
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- added copper zone on In2.Cu, net +3V3
- added copper zone on B.Cu, net GND
- added copper zone on F.Cu, net GND
- added copper zone on In1.Cu, net GND
- added copper zone on B.Cu, net MODEM_3.3V
- added copper zone on F.Cu, net MODEM_3.3V
- removed copper zone on F.Cu, net (none)
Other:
- board text added: "Ground Polygons!"
